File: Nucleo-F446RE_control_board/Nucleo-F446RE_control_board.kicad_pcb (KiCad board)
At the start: 2 copper layers, 100 x 90 mm, 51 parts, among them J1 Conn_01x02_Pin, J10 Conn_01x03_Pin, J11 Conn_01x03_Pin, J12 Conn_01x03_Pin, J13 Conn_01x04_Pin, J14 Conn_01x02_Pin, J15 Conn_01x02_Pin, J16 Conn_01x02_Pin, J2 Conn_01x03_Pin, J3 Conn_01x03_Pin, J4 Conn_01x03_Pin, J5 Conn_01x03_Pin, J6 Conn_01x03_Pin, J7 Conn_01x02_Pin, J8 Conn_01x02_Pin, J9 Conn_01x04_Pin, U2 MCP2562-E-P, U3 MCP2562-E-P

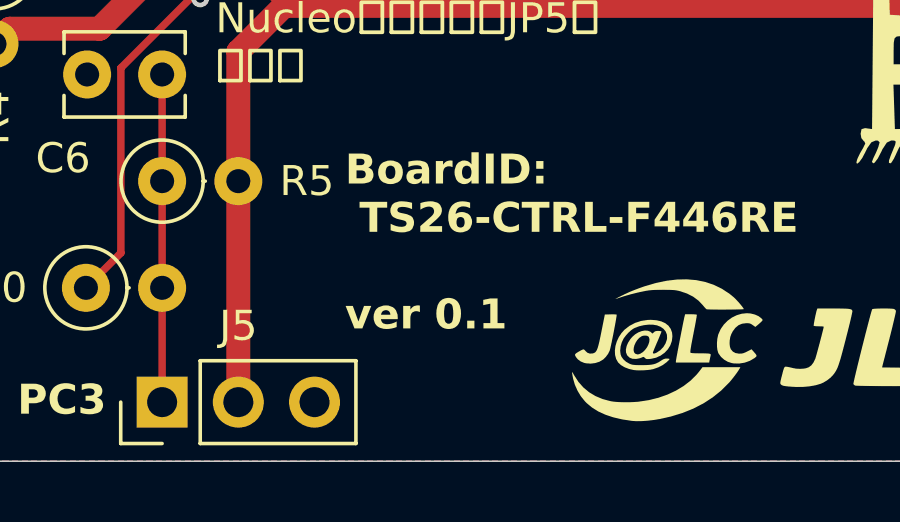
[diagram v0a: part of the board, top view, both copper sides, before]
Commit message: F446RE基板　ねじ下のベタを除去，ver 0.2
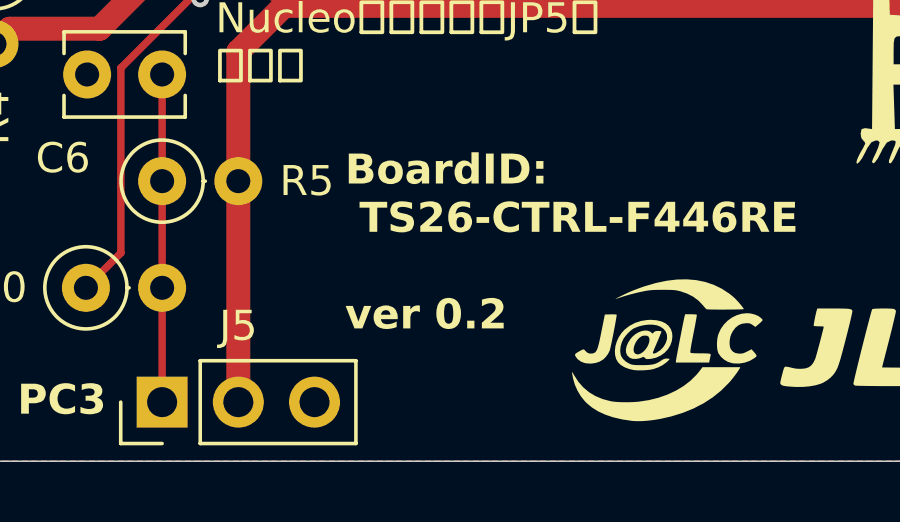
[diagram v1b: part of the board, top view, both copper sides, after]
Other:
- board text added: "BoardID: TS26-CTRL-F446RE ver 0.2"
- board text removed: "BoardID: TS26-CTRL-F446RE ver 0.1"
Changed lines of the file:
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@@
 		)
 	)
-	(gr_text "BoardID:\n TS26-CTRL-F446RE\n\nver 0.1"
+	(gr_text "BoardID:\n TS26-CTRL-F446RE\n\nver 0.2"
 		(at 45.974 107.696 0)
 		(layer "F.SilkS")
@@
 	)
 	(zone
+		(layers "F.Cu" "B.Cu")
+		(hatch edge 0.5)
+		(connect_pads yes
+			(clearance 0)
+		)
+		(min_thickness 0.25)
+		(keepout
+			(tracks allowed)
+			(vias allowed)
+			(pads allowed)
+			(copperpour not_allowed)
+			(footprints allowed)
+		)
+		(placement
+			(enabled no)
+			(sheetname "")
+		)
+		(fill
+			(thermal_gap 0.5)
+			(thermal_bridge_width 0.5)
+			(island_removal_mode 0)
+		)
+		(polygon
+			(pts
+				(xy 25 25) (xy 33 25) (xy 33 33) (xy 25 33)
+			)
+		)
+	)
+	(zone
+		(layers "F.Cu" "B.Cu")
+		(hatch edge 0.5)
+		(connect_pads yes
+			(clearance 0)
+		)
+		(min_thickness 0.25)
+		(keepout
+			(tracks allowed)
+			(vias allowed)
+			(pads allowed)
+			(copperpour not_allowed)
+			(footprints allowed)
+		)
+		(placement
+			(enabled no)
+			(sheetname "")
+		)
+		(fill
+			(thermal_gap 0.5)
+			(thermal_bridge_width 0.5)
+			(island_removal_mode 0)
+		)
+		(polygon
+			(pts
+				(xy 117 107) (xy 125 107) (xy 125 115) (xy 117 115)
+			)
+		)
+	)
+	(zone
 		(net "GND")
 		(layers "F.Cu" "B.Cu")
@@
 			)
 		)
+	)
+	(zone
+		(layers "F.Cu" "B.Cu")
+		(hatch edge 0.5)
+		(connect_pads yes
+			(clearance 0)
+		)
+		(min_thickness 0.25)
+		(keepout
+			(tracks allowed)
+			(vias allowed)
+			(pads allowed)
+			(copperpour not_allowed)
+			(footprints allowed)
+		)
+		(placement
+			(enabled no)
+			(sheetname "")
+		)
+		(fill
+			(thermal_gap 0.5)
+			(thermal_bridge_width 0.5)
+			(island_removal_mode 0)
+		)
+		(polygon
+			(pts
+				(xy 25 107) (xy 33 107) (xy 33 115) (xy 25 115)
+			)
+		)
+	)
+	(zone
+		(layers "F.Cu" "B.Cu")
+		(hatch edge 0.5)
+		(connect_pads yes
+			(clearance 0)
+		)
+		(min_thickness 0.25)
+		(keepout
+			(tracks allowed)
+			(vias allowed)
+			(pads allowed)
+			(copperpour not_allowed)
+			(footprints allowed)
+		)
+		(placement
+			(enabled no)
+			(sheetname "")
+		)
+		(fill
+			(thermal_gap 0.5)
+			(thermal_bridge_width 0.5)
+			(island_removal_mode 0)
+		)
+		(polygon
+			(pts
+				(xy 117 25) (xy 125 25) (xy 125 33) (xy 117 33)
+			)
+		)

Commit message: F446RE基板　シリアルサーボ用端子を4ピンに変更，GNDベタにビアを追加，ver 0.3
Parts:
- G***: moved to B.Cu
- J14: value Conn_01x02_Pin -> Conn_01x04_Pin; footprint OU_connector:DF1E-2P-2.5DS -> OU_connector:DF1E-4P-2.5DS
- moved G*** 13.8 mm to (67.0, 85.0), turned to 180 degrees
- moved J16 9.91 mm to (113.5, 101.1)
- moved C10 3.46 mm to (109.7, 96.0), turned to 90 degrees
- moved J14 0.80 mm to (114.3, 78.7)
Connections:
- J14 pad 1: +3.3V -> GND
- U1 pad CN10_33: unconnected-(U1-PA10-PadCN10_33) -> /PA10
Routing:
- net /PA10: track 0.00 -> 19.0 mm
- net +3.3V: track 310.7 -> 328.7 mm
- net /CAN2-: track 16.3 -> 25.9 mm
- net /CAN2+: track 20.4 -> 29.1 mm
- net /PB14: track 44.1 -> 45.6 mm
- net /PA9: track 29.5 -> 30.3 mm
- net GND: vias 1 -> 228
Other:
- board text added: "BoardID: TS26-CTRL-F446RE ver 0.3"
- board text removed: "BoardID: TS26-CTRL-F446RE ver 0.2"

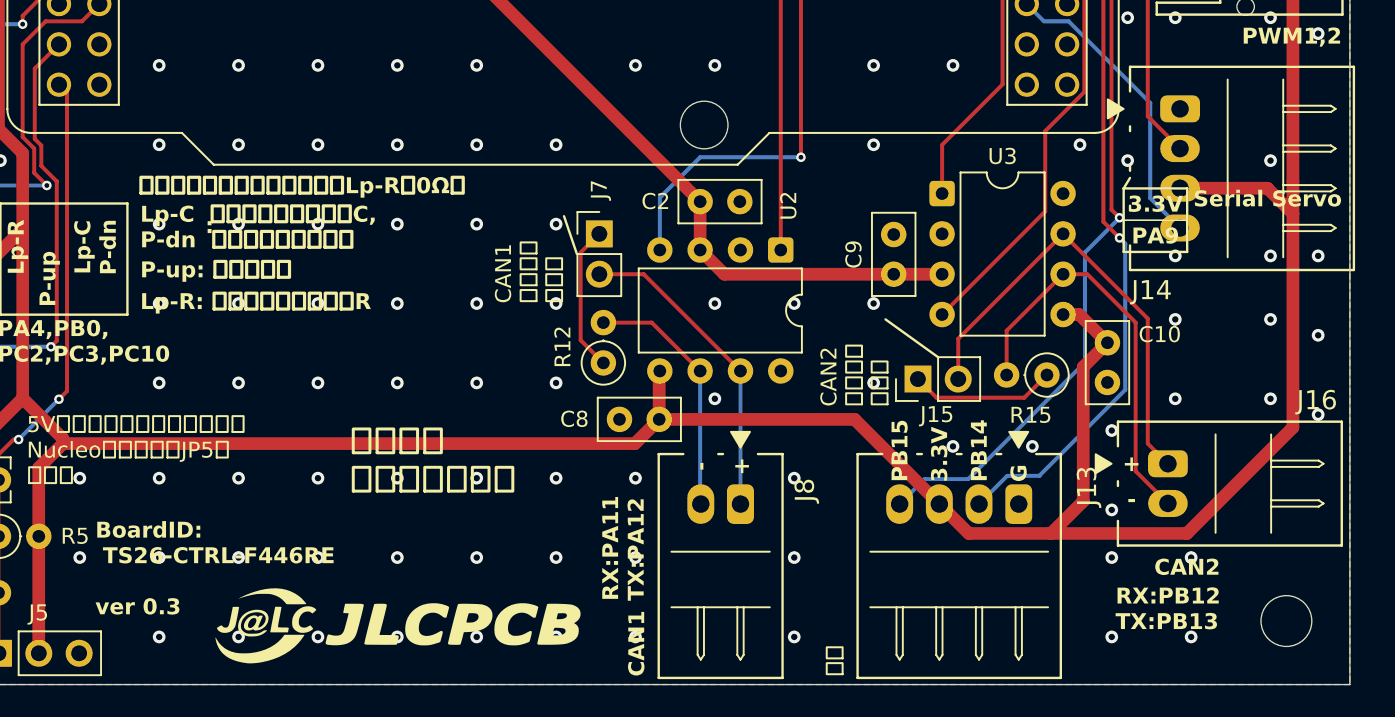
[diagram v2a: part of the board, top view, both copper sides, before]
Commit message: F446RE基板　シリアルサーボ端子のシルクを修正，ver 0.4
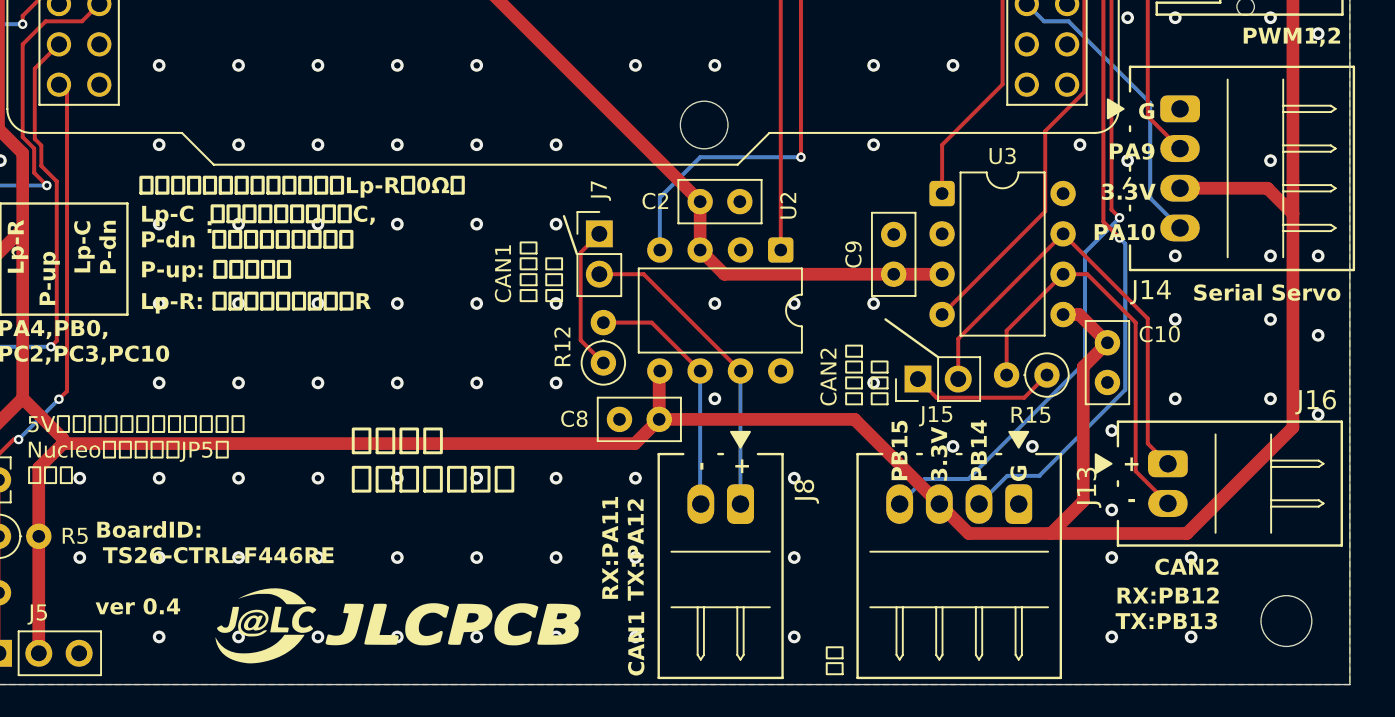
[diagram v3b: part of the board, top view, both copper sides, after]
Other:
- board text added: "BoardID: TS26-CTRL-F446RE ver 0.4"
- board text added: "PA10"
- board text removed: "BoardID: TS26-CTRL-F446RE ver 0.3"
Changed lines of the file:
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@@
-	)
-	(gr_rect
-		(start 110.75 83.75)
-		(end 114.75 87.75)
-		(stroke
-			(width 0.15)
-			(type solid)
-		)
-		(fill no)
-		(layer "F.SilkS")
 	)
 	(gr_rect
@@
 			(width 0.15)
 			(type solid)
-		)
-		(layer "F.SilkS")
-	)
-	(gr_line
-		(start 114.75 85.75)
-		(end 110.75 85.75)
-		(stroke
-			(width 0.1)
-			(type default)
 		)
 		(layer "F.SilkS")
@@
 		)
 	)
-	(gr_text "BoardID:\n TS26-CTRL-F446RE\n\nver 0.3"
+	(gr_text "BoardID:\n TS26-CTRL-F446RE\n\nver 0.4"
 		(at 45.974 107.696 0)
 		(layer "F.SilkS")
@@
 		)
 	)
-	(gr_text "3.3V"
-		(at 112.75 84.75 0)
-		(layer "F.SilkS")
-		(effects
-			(font
-				(size 1 1)
-				(thickness 0.2)
-				(bold yes)
-			)
-		)
-	)
-	(gr_text "PA9"
-		(at 112.75 86.75 0)
-		(layer "F.SilkS")
-		(effects
-			(font
-				(size 1 1)
-				(thickness 0.2)
-				(bold yes)
-			)
-		)
-	)
 	(gr_text "GND"
 		(at 113 26.5 0)
@@
 		)
 	)
+	(gr_text "G"
+		(at 112.776 79.502 0)
+		(layer "F.SilkS" knockout)
+		(effects
+			(font
+				(size 1 1)
+				(thickness 0.2)
+				(bold yes)
+			)
+			(justify right bottom)
+		)
+	)
+	(gr_text "PA9"
+		(at 112.776 82.042 0)
+		(layer "F.SilkS" knockout)
+		(effects
+			(font
+				(size 1 1)
+				(thickness 0.2)
+				(bold yes)
+			)
+			(justify right bottom)
+		)
+	)
+	(gr_text "3.3V"
+		(at 112.776 84.582 0)
+		(layer "F.SilkS" knockout)
+		(effects
+			(font
+				(size 1 1)
+				(thickness 0.2)
+				(bold yes)
+			)
+			(justify right bottom)
+		)
+	)
+	(gr_text "PA10"
+		(at 112.776 87.122 0)
+		(layer "F.SilkS" knockout)
+		(effects
+			(font
+				(size 1 1)
+				(thickness 0.2)
+				(bold yes)
+			)
+			(justify right bottom)
+		)
+	)
 	(gr_text "PC8"
 		(at 114.5 56.5 0)
@@
 		)
 	)
+	(gr_text "Serial Servo"
+		(at 124.46 90.932 0)
+		(layer "F.SilkS" knockout)
+		(effects
+			(font
+				(size 1 1)
+				(thickness 0.2)
+				(bold yes)
+			)
+			(justify right bottom)
+		)
+	)
 	(gr_text "PWM3,4"
 		(at 124.5 63.75 0)
@@
 		(layer "F.SilkS" knockout)
 		(effects
-			(font
-				(size 1 1)
-				(thickness 0.2)
-				(bold yes)
-			)
-			(justify right bottom)
-		)
-	)
-	(gr_text "Serial Servo"
-		(at 124.5 85 0)
-		(layer "F.SilkS" knockout)
-		(effects

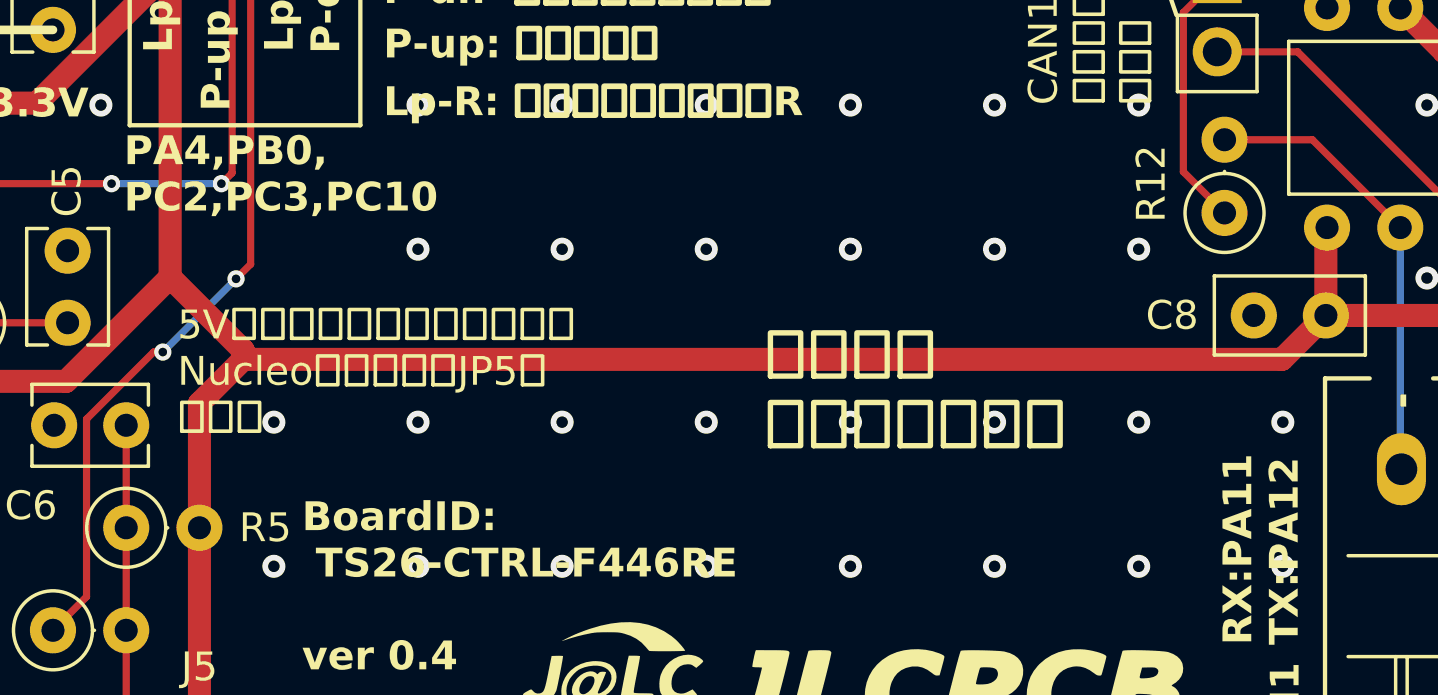
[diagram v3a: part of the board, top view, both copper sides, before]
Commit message: F446RE基板　予備GPIOのシルクを追加，ver 0.5
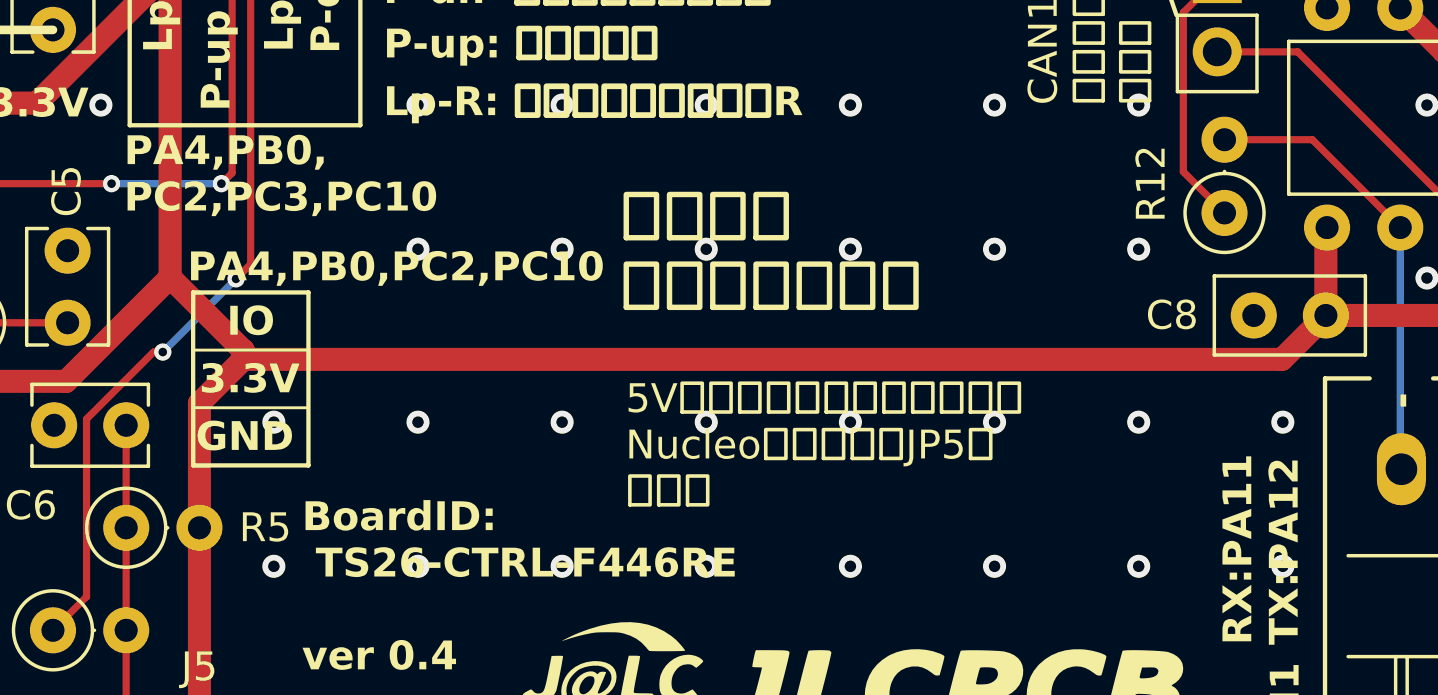
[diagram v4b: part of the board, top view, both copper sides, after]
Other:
- board text added: "PA4,PB0,PC2,PC10"
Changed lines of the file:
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@@
+		(layer "F.SilkS")
+	)
+	(gr_rect
+		(start 42.2 97.5)
+		(end 46.2 103.5)
+		(stroke
+			(width 0.15)
+			(type solid)
+		)
+		(fill no)
+		(layer "F.SilkS")
+	)
+	(gr_line
+		(start 46.2 99.5)
+		(end 42.2 99.5)
+		(stroke
+			(width 0.1)
+			(type default)
+		)
+		(layer "F.SilkS")
+	)
+	(gr_line
+		(start 46.2 101.5)
+		(end 42.2 101.5)
+		(stroke
+			(width 0.1)
+			(type default)
+		)
 		(layer "F.SilkS")
 	)
@@
 	)
 	(gr_text "5V電源入力を使用する場合，\nNucleoボード上のJP5を\n要確認"
-		(at 41.656 98.044 0)
+		(at 57.2 100.6 0)
 		(layer "F.SilkS")
 		(effects
@@
 		)
 	)
+	(gr_text "PA4,PB0,PC2,PC10"
+		(at 42 97.2 0)
+		(layer "F.SilkS" knockout)
+		(effects
+			(font
+				(size 1 1)
+				(thickness 0.2)
+				(bold yes)
+			)
+			(justify left bottom)
+		)
+	)
 	(gr_text "Pull-up\nResistor"
 		(at 117.856 53.086 0)
@@
 		)
 	)
+	(gr_text "IO"
+		(at 44.2 98.5 0)
+		(layer "F.SilkS")
+		(effects
+			(font
+				(size 1 1)
+				(thickness 0.2)
+				(bold yes)
+			)
+		)
+	)
 	(gr_text "+"
 		(at 111.252 101.092 0)
@@
 		)
 	)
+	(gr_text "GND"
+		(at 45.7 102.5 0)
+		(layer "F.SilkS")
+		(effects
+			(font
+				(size 1 1)
+				(thickness 0.2)
+				(bold yes)
+			)
+			(justify right)
+		)
+	)
+	(gr_text "3.3V"
+		(at 45.9 100.5 0)
+		(layer "F.SilkS")
+		(effects
+			(font
+				(size 1 1)
+				(thickness 0.2)
+				(bold yes)
+			)
+			(justify right)
+		)
+	)
 	(gr_text "PB8"
 		(at 112.75 39 0)
@@
 	)
 	(gr_text "岡山大学\nロボット研究会"
-		(at 62 103 0)
-		(layer "F.SilkS")
-		(effects
+		(at 57 98.2 0)
+		(layer "F.SilkS")
+		(effects

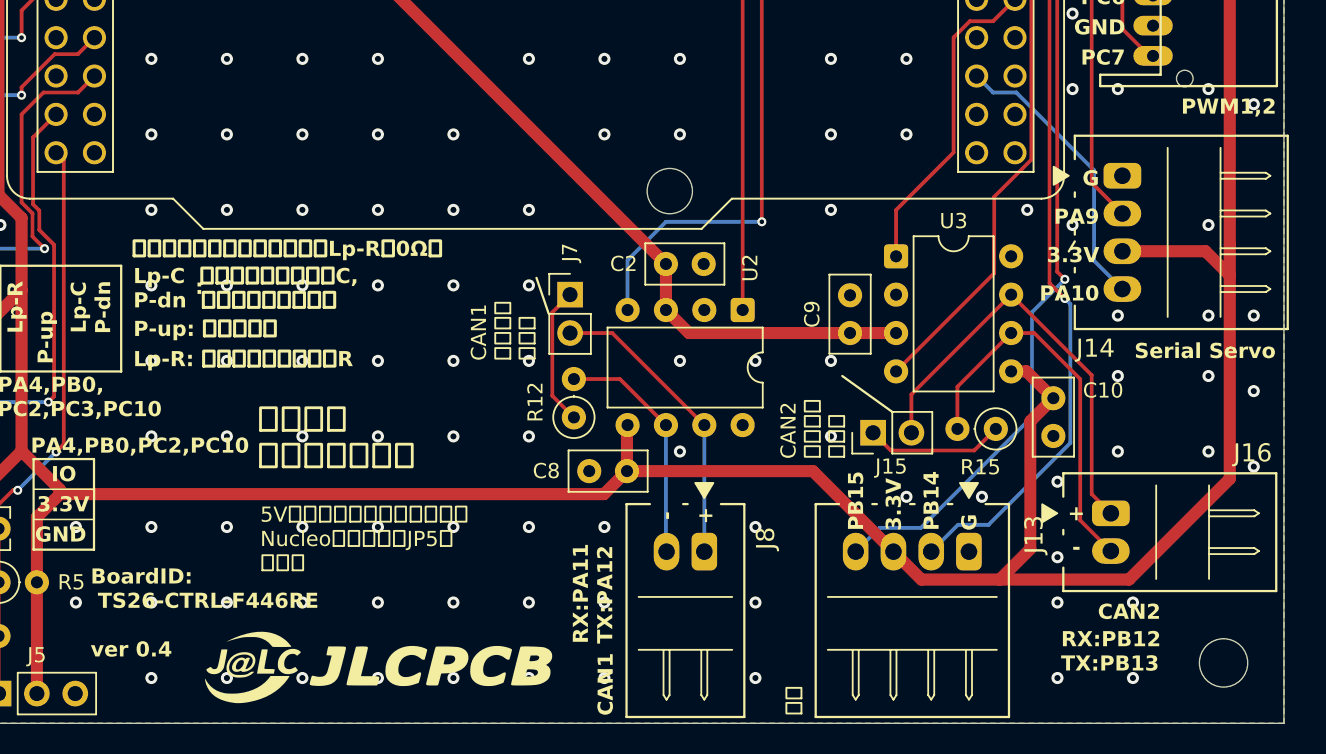
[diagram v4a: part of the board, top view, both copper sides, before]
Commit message: F446RE基板　シリアル通信端子の電源ピンを5Vに変更，ver 0.5
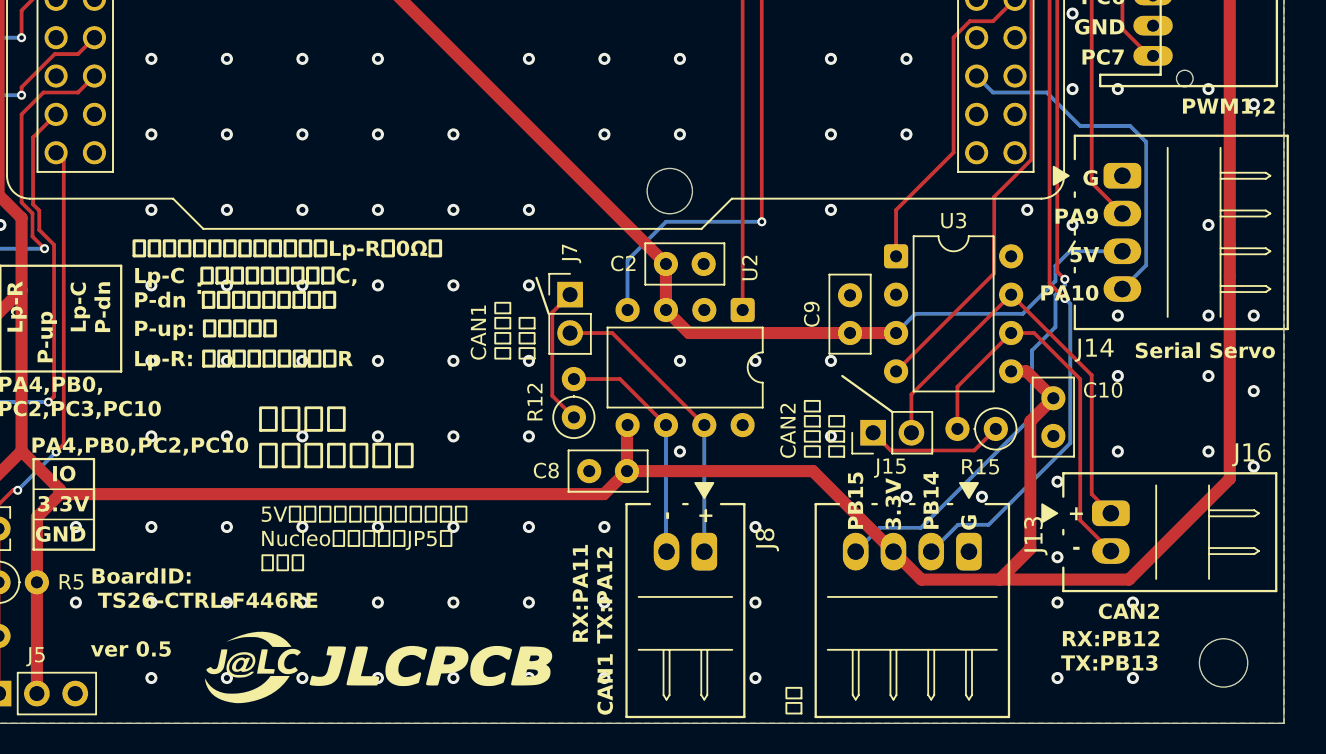
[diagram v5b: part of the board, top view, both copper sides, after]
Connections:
- J14 pad 3: +3.3V -> +5V
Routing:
- net +5V: track 114.5 -> 132.3 mm
- net +3.3V: track 328.7 -> 320.9 mm
- net /PA10: track 19.0 -> 23.4 mm
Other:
- board text added: "5V"
- board text added: "BoardID: TS26-CTRL-F446RE ver 0.5"
- board text removed: "BoardID: TS26-CTRL-F446RE ver 0.4"
